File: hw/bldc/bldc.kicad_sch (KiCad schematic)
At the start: 67 parts, among them IC1 MP2315SGJ-P, J1 Conn_01x05, J3 Conn_01x06, J4 Conn_01x04, Q1 BSC13DN30NSFD, Q10 BSC13DN30NSFD, Q2 BSC13DN30NSFD, Q7 BSC13DN30NSFD, Q8 BSC13DN30NSFD, Q9 BSC13DN30NSFD, U2 IR2101, U3 IR2101, U4 IR2101, U5 STM32L431CCTx

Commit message: pcb update
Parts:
- removed C6: 0.1uF, symbol Device:C
- removed J4: Conn_01x04, symbol Connector_Generic:Conn_01x04
- added R9: 4K7, Resistor_SMD:R_0603_1608Metric, symbol Device:R_US
- added TP6, TP7, TP8, TP9: SP, TestPoint:TestPoint_Pad_3.0x3.0mm, symbol Connector:TestPoint
- added U1: LD1117S33TR_SOT223, Package_TO_SOT_SMD:SOT-223-3_TabPin2, symbol Regulator_Linear:LD1117S33TR_SOT223
- C1, C11, C12, C13, C15, C16, C17, C3, C4, C5, C9: footprint (none) -> Capacitor_SMD:C_0603_1608Metric
- C10, C7, C8: value 0.1uF -> 10nF; footprint (none) -> Capacitor_SMD:C_0603_1608Metric
- C14, C2: value 0.1uF -> 10uF; footprint (none) -> Capacitor_SMD:C_0603_1608Metric
- D4: footprint (none) -> LED_SMD:LED_0603_1608Metric
- IC1: footprint SOT65P280X100-8N -> _MAYANK:MP2315SGJ
- J1: footprint (none) -> Connector_PinHeader_2.00mm:PinHeader_1x05_P2.00mm_Vertical
- J3: footprint (none) -> Connector_PinHeader_2.54mm:PinHeader_1x06_P2.54mm_Vertical
- L1: footprint (none) -> Inductor_SMD:L_Neosid_SM-PIC0512H
- R1, R10, R11, R12, R13, R14, R15, R16, R18, R19, R2, R20, R21, R22, R23, R24, R25, R26, R27, R28, R3, R4, R5, R6, R7: footprint (none) -> Resistor_SMD:R_0603_1608Metric
- R17: value 0R -> 33K; footprint (none) -> Resistor_SMD:R_0603_1608Metric
- TP1, TP2, TP3, TP4, TP5: footprint (none) -> _MAYANK:SOLDERPAD6x4
- U2, U3, U4: footprint (none) -> Package_SO:SOIC-8_3.9x4.9mm_P1.27mm
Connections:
- net VIN is gone; now on net VDC: TP4.1
- net +3V3: now also C1.2, TP6.1, U1.2 (VO); no longer C14.2, L1.2, R12.1
- net GND: now also C1.1, C4.2, R9.2, TP9.1, U1.1 (GND)
- net PHASE_A: no longer C1.2
- net PHASE_B: no longer C4.2
- net VDC: now also C9.1, IC1.2 (IN), R17.2; no longer R17.1
- net VDD: now also C14.2, L1.2, R12.1, U1.3 (VI); no longer C9.1, IC1.2 (IN), R17.2
- net at R18.2: now also TP7.1
- net at C17.2, R7.2: now also TP8.1
- net at C2.1, D1.1 (K), U2.8 (VB): no longer C1.1
- net ADC_VDC: now reaches U5.15 (PA5)
- net ADC_VDC: now also C4.1, R17.1, R9.1
- net at C3.1, D2.1 (K), U3.8 (VB): no longer C4.1
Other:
- moved on the sheet: C11, C14, C15, C16, C17, C3, C5, D4, J1, J3, R10, R18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

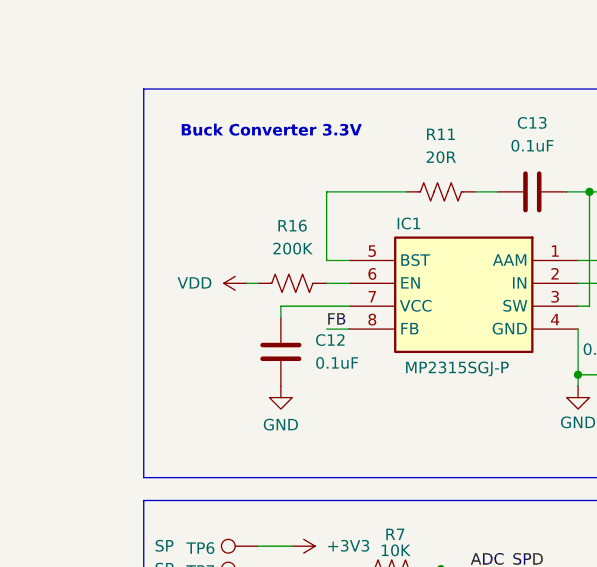
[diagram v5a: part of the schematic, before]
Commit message: component placement
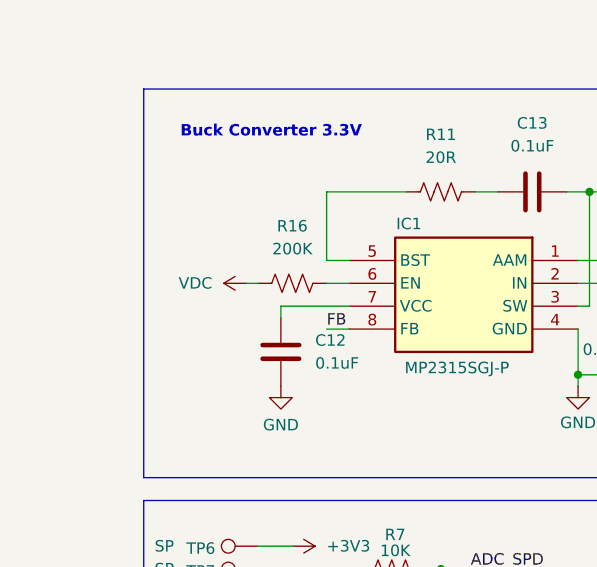
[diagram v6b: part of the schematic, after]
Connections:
- net VDC: now also R16.1
- net VDD: no longer R16.1

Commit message: pcb routing update
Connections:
- net LED: now also U5.32 (PA11); no longer U5.28 (PB15)
- net TIM1_CH1: now also U4.2 (HIN); no longer U2.2 (HIN)
- net TIM1_CH1N: now also U4.3 (LIN); no longer U2.3 (LIN)
- net TIM1_CH3: now also U2.2 (HIN); no longer U4.2 (HIN)
- net TIM1_CH3N: now also U2.3 (LIN); no longer U4.3 (LIN)
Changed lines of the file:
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@@
-	(wire
-		(pts
-			(xy 24.13 176.53) (xy 30.48 176.53)
-		)
-		(stroke
-			(width 0)
-			(type default)
-		)
-	)
 	(wire
 		(pts
@@
 		(pts
 			(xy 158.75 88.9) (xy 170.18 88.9)
+		)
+		(stroke
+			(width 0)
+			(type default)
+		)
+	)
+	(wire
+		(pts
+			(xy 67.31 140.97) (xy 60.96 140.97)
 		)
 		(stroke
@@
 		)
 	)
-	(label "TIM1_CH3"
-		(at 158.75 137.16 0)
-		(fields_autoplaced yes)
-		(effects
-			(font
-				(size 1.27 1.27)
-			)
-			(justify left bottom)
-		)
-	)
 	(label "PHASE_C"
 		(at 223.52 142.24 180)
@@
 		)
 	)
+	(label "TIM1_CH3N"
+		(at 158.75 40.64 0)
+		(fields_autoplaced yes)
+		(effects
+			(font
+				(size 1.27 1.27)
+			)
+			(justify left bottom)
+		)
+	)
 	(label "SWDIO"
 		(at 114.3 181.61 180)
@@
 		)
 	)
+	(label "LED"
+		(at 67.31 140.97 180)
+		(fields_autoplaced yes)
+		(effects
+			(font
+				(size 1.27 1.27)
+			)
+			(justify right bottom)
+		)
+	)
 	(label "SWCLK"
 		(at 114.3 176.53 180)
@@
 		)
 	)
-	(label "TIM1_CH1"
-		(at 158.75 38.1 0)
-		(fields_autoplaced yes)
-		(effects
-			(font
-				(size 1.27 1.27)
-			)
-			(justify left bottom)
-		)
-	)
 	(label "ADC_B"
 		(at 237.49 104.14 0)
@@
 		)
 	)
+	(label "TIM1_CH1N"
+		(at 158.75 139.7 0)
+		(fields_autoplaced yes)
+		(effects
+			(font
+				(size 1.27 1.27)
+			)
+			(justify left bottom)
+		)
+	)
 	(label "ADC_C"
 		(at 237.49 144.78 0)
@@
 		)
 	)
-	(label "TIM1_CH1N"
-		(at 158.75 40.64 0)
-		(fields_autoplaced yes)
-		(effects
-			(font
-				(size 1.27 1.27)
-			)
-			(justify left bottom)
-		)
-	)
 	(label "TIM1_CH2N"
 		(at 158.75 91.44 0)
@@
 		)
 	)
-	(label "LED"
-		(at 24.13 176.53 0)
-		(fields_autoplaced yes)
-		(effects
-			(font
-				(size 1.27 1.27)
-			)
-			(justify left bottom)
-		)
-	)
 	(label "ADC_C"
 		(at 72.39 118.11 180)
@@
 		)
 	)
+	(label "TIM1_CH1"
+		(at 158.75 137.16 0)
+		(fields_autoplaced yes)
+		(effects
+			(font
+				(size 1.27 1.27)
+			)
+			(justify left bottom)
+		)
+	)
+	(label "TIM1_CH3"
+		(at 158.75 38.1 0)
+		(fields_autoplaced yes)
+		(effects
+			(font
+				(size 1.27 1.27)
+			)
+			(justify left bottom)
+		)
+	)
 	(label "FB"
 		(at 36.83 41.91 0)
@@
 		)
 	)
-	(label "TIM1_CH3N"
-		(at 158.75 139.7 0)
-		(fields_autoplaced yes)
-		(effects
-			(font
-				(size 1.27 1.27)
-			)
-			(justify left bottom)
-		)
-	)

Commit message: pcb update
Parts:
- added TP10, TP11: C, TestPoint:TestPoint_Pad_D1.0mm, symbol Connector:TestPoint
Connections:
- net at U5.25 (PB12): now also TP10.1
- net at U5.27 (PB14): now also TP11.1
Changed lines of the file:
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@@
 	(wire
 		(pts
+			(xy 27.94 173.99) (xy 30.48 173.99)
+		)
+		(stroke
+			(width 0)
+			(type default)
+		)
+	)
+	(wire
+		(pts
 			(xy 60.96 146.05) (xy 72.39 146.05)
 		)
@@
 	(wire
 		(pts
+			(xy 27.94 168.91) (xy 30.48 168.91)
+		)
+		(stroke
+			(width 0)
+			(type default)
+		)
+	)
+	(wire
+		(pts
 			(xy 19.05 156.21) (xy 30.48 156.21)
 		)
@@
 	(symbol
 		(lib_id "Connector:TestPoint")
+		(at 27.94 173.99 90)
+		(unit 1)
+		(exclude_from_sim no)
+		(in_bom yes)
+		(on_board yes)
+		(dnp no)
+		(property "Reference" "TP11"
+			(at 22.86 175.2601 90)
+			(effects
+				(font
+					(size 1.27 1.27)
+				)
+				(justify left)
+			)
+		)
+		(property "Value" "C"
+			(at 22.86 172.7201 90)
+			(effects
+				(font
+					(size 1.27 1.27)
+				)
+				(justify left)
+			)
+		)
+		(property "Footprint" "TestPoint:TestPoint_Pad_D1.0mm"
+			(at 27.94 168.91 0)
+			(effects
+				(font
+					(size 1.27 1.27)
+				)
+				(hide yes)
+			)
+		)
+		(property "Datasheet" "~"
+			(at 27.94 168.91 0)
+			(effects
+				(font
+					(size 1.27 1.27)
+				)
+				(hide yes)
+			)
+		)
+		(property "Description" "test point"
+			(at 27.94 173.99 0)
+			(effects
+				(font
+					(size 1.27 1.27)
+				)
+				(hide yes)
+			)
+		)
+		(pin "1"
+		)
+		(instances
+			(project "bldc"
+				(path "/8f50835c-fbe0-401c-8ea4-1e9972c1e8f7"
+					(reference "TP11")
+					(unit 1)
+				)
+			)
+		)
+	)
+	(symbol
+		(lib_id "Connector:TestPoint")
 		(at 29.21 73.66 90)
 		(unit 1)
@@
 					(unit 1)
 				)
+			)
+		)
+	)
+	(symbol
+		(lib_id "Connector:TestPoint")
+		(at 27.94 168.91 90)
+		(unit 1)
+		(exclude_from_sim no)
+		(in_bom yes)
+		(on_board yes)
+		(dnp no)
+		(property "Reference" "TP10"
+			(at 22.86 170.1801 90)
+			(effects
+				(font
+					(size 1.27 1.27)
+				)
+				(justify left)
+			)
+		)
+		(property "Value" "C"
+			(at 22.86 167.6401 90)
+			(effects
+				(font
+					(size 1.27 1.27)
+				)
+				(justify left)
+			)
+		)
+		(property "Footprint" "TestPoint:TestPoint_Pad_D1.0mm"
+			(at 27.94 163.83 0)
+			(effects
+				(font
+					(size 1.27 1.27)
+				)
+				(hide yes)
+			)
+		)
+		(property "Datasheet" "~"
+			(at 27.94 163.83 0)
+			(effects
+				(font
+					(size 1.27 1.27)
+				)
+				(hide yes)
+			)
+		)
+		(property "Description" "test point"
+			(at 27.94 168.91 0)
+			(effects
+				(font
+					(size 1.27 1.27)
+				)
+				(hide yes)
+			)
+		)
+		(pin "1"
+		)
+		(instances
+			(project "bldc"
+				(path "/8f50835c-fbe0-401c-8ea4-1e9972c1e8f7"
+					(reference "TP10")
+					(unit 1)
+				)
